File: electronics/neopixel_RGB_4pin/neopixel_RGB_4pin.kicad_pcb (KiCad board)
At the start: 2 copper layers, 9 x 9 mm, 6 parts, among them J1 Conn_01x03, J2 Conn_01x03

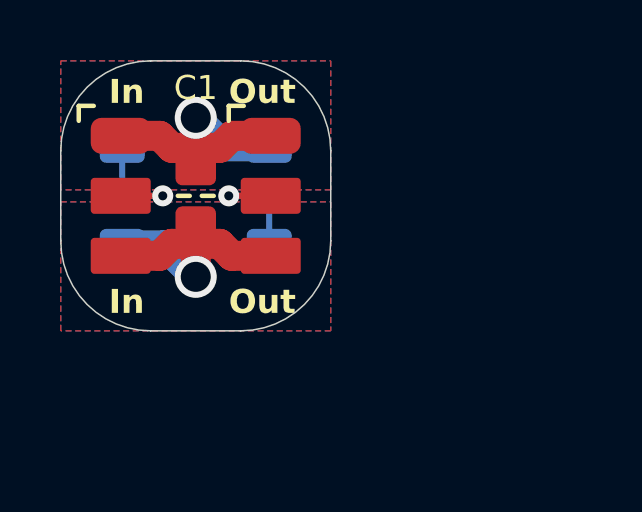
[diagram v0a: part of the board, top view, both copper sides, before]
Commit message: updated labels
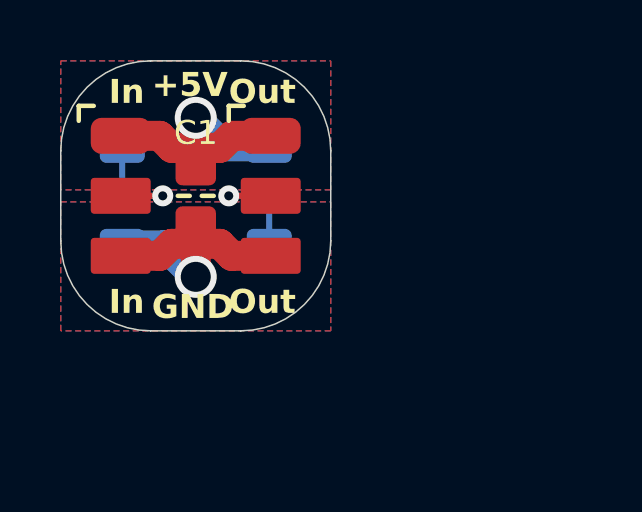
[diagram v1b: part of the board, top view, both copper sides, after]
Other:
- board text added: "+5V"
- board text added: "GND"
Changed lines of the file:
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@@
     (property "ki_keywords" "cap capacitor")
     (attr smd)
-    (fp_text reference "C1" (at -3.6 0 -180) (layer "F.SilkS")
+    (fp_text reference "C1" (at -2.1 0 -180) (layer "F.SilkS")
         (effects (font (size 0.8 0.8) (thickness 0.15)))
     )
@@
     (property "Sheetname" "")
     (attr smd)
-    (fp_text reference "U1" (at 0 6.5 unlocked) (layer "B.SilkS")
+    (fp_text reference "U1" (at 2.5 3.3 unlocked) (layer "B.SilkS")
         (effects (font (size 0.8 0.8) (thickness 0.15)) (justify mirror))
     )
@@
     (effects (font (size 0.8 0.8) (thickness 0.15) bold) (justify left bottom))
   )
+  (gr_text "GND" (at 114.4 79.2) (layer "F.SilkS")
+    (effects (font (size 0.8 0.8) (thickness 0.15) bold))
+  )
   (gr_text "Out" (at 115.6 79.5) (layer "F.SilkS")
     (effects (font (size 0.8 0.8) (thickness 0.15) bold) (justify left bottom))
   )
+  (gr_text "+5V" (at 114.3 71.8) (layer "F.SilkS")
+    (effects (font (size 0.8 0.8) (thickness 0.15) bold))
+  )
   (segment (start 114.5 73.9) (end 115.3 73.9) (width 1) (layer "F.Cu") (net 1))
